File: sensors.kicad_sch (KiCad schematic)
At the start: 7 parts

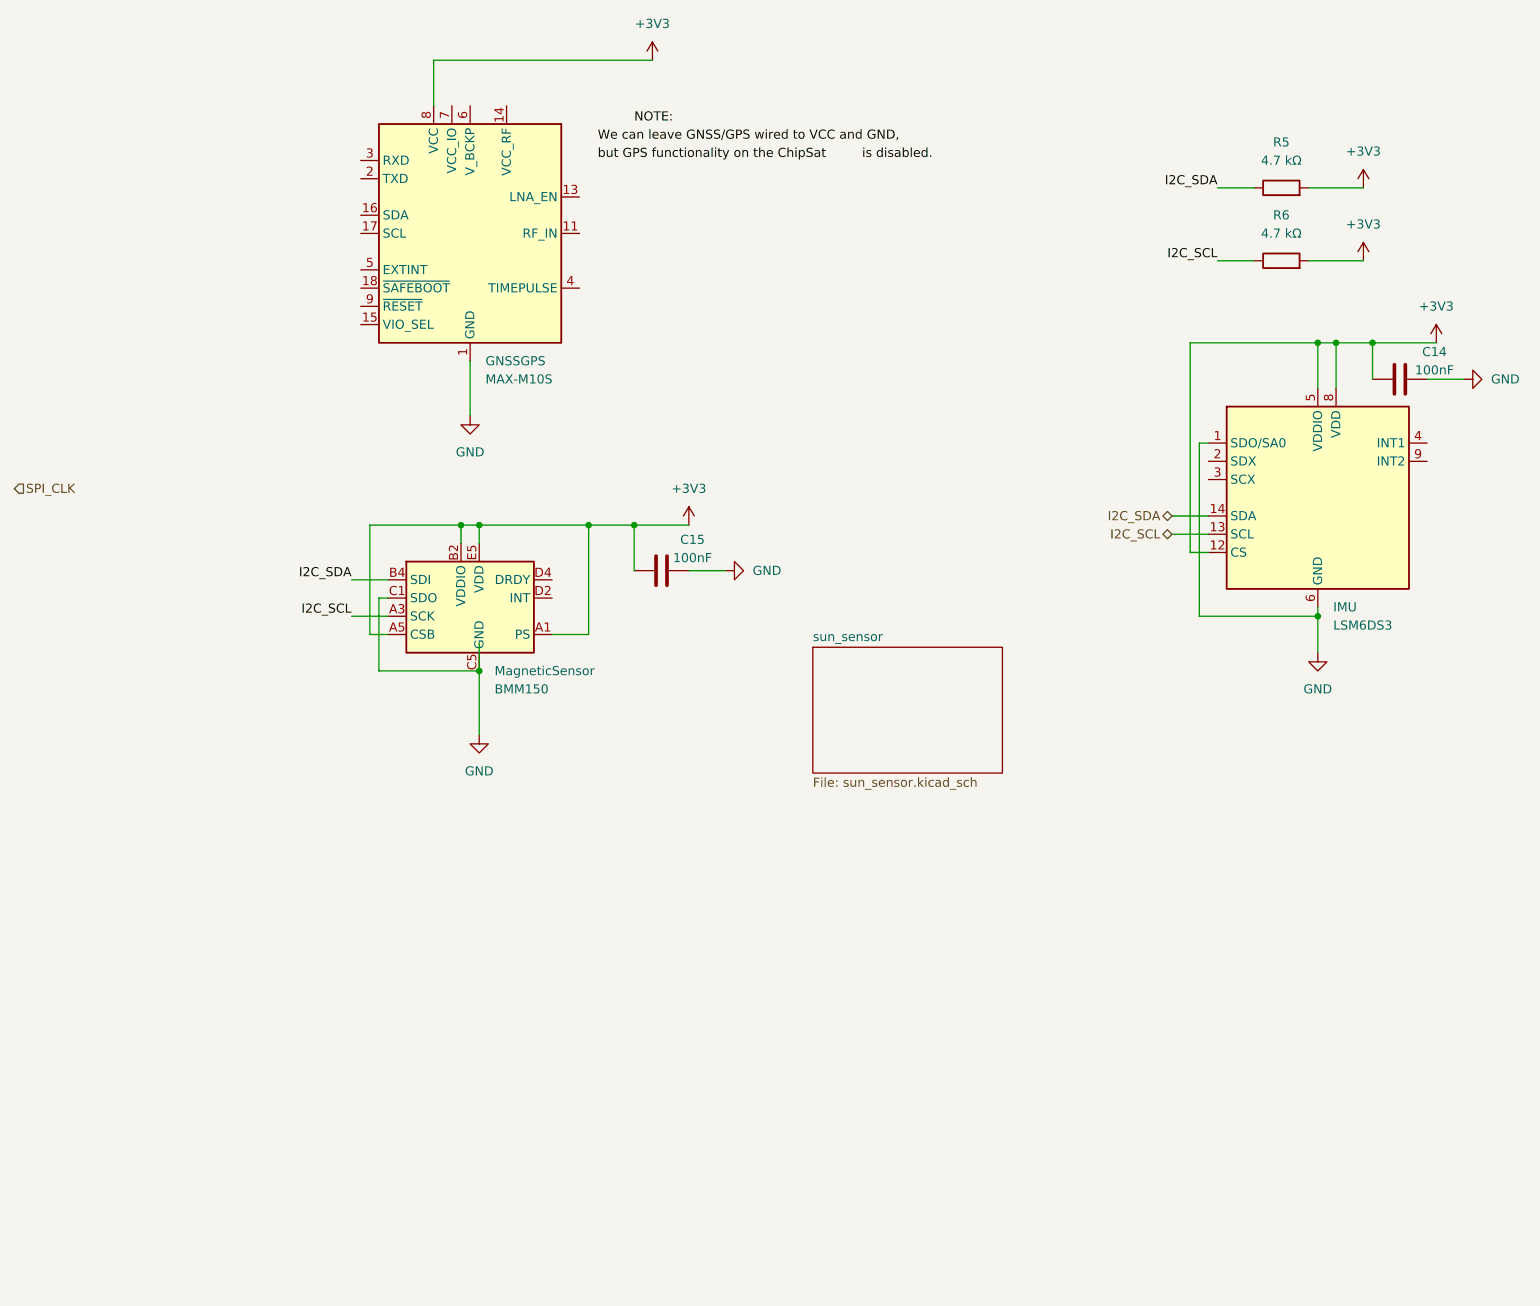
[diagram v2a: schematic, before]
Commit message: Updated GPS, BMI, LSM, and BNO on sensors. Added hierachical labels and new "golden rule" connections
Updated each sensor ensuring they followed the golden rule. I also added hiearchical labels to the topsheet and the inside sheets. Fixed specific sensors to be in SPI vs I2C mode and updated the names.
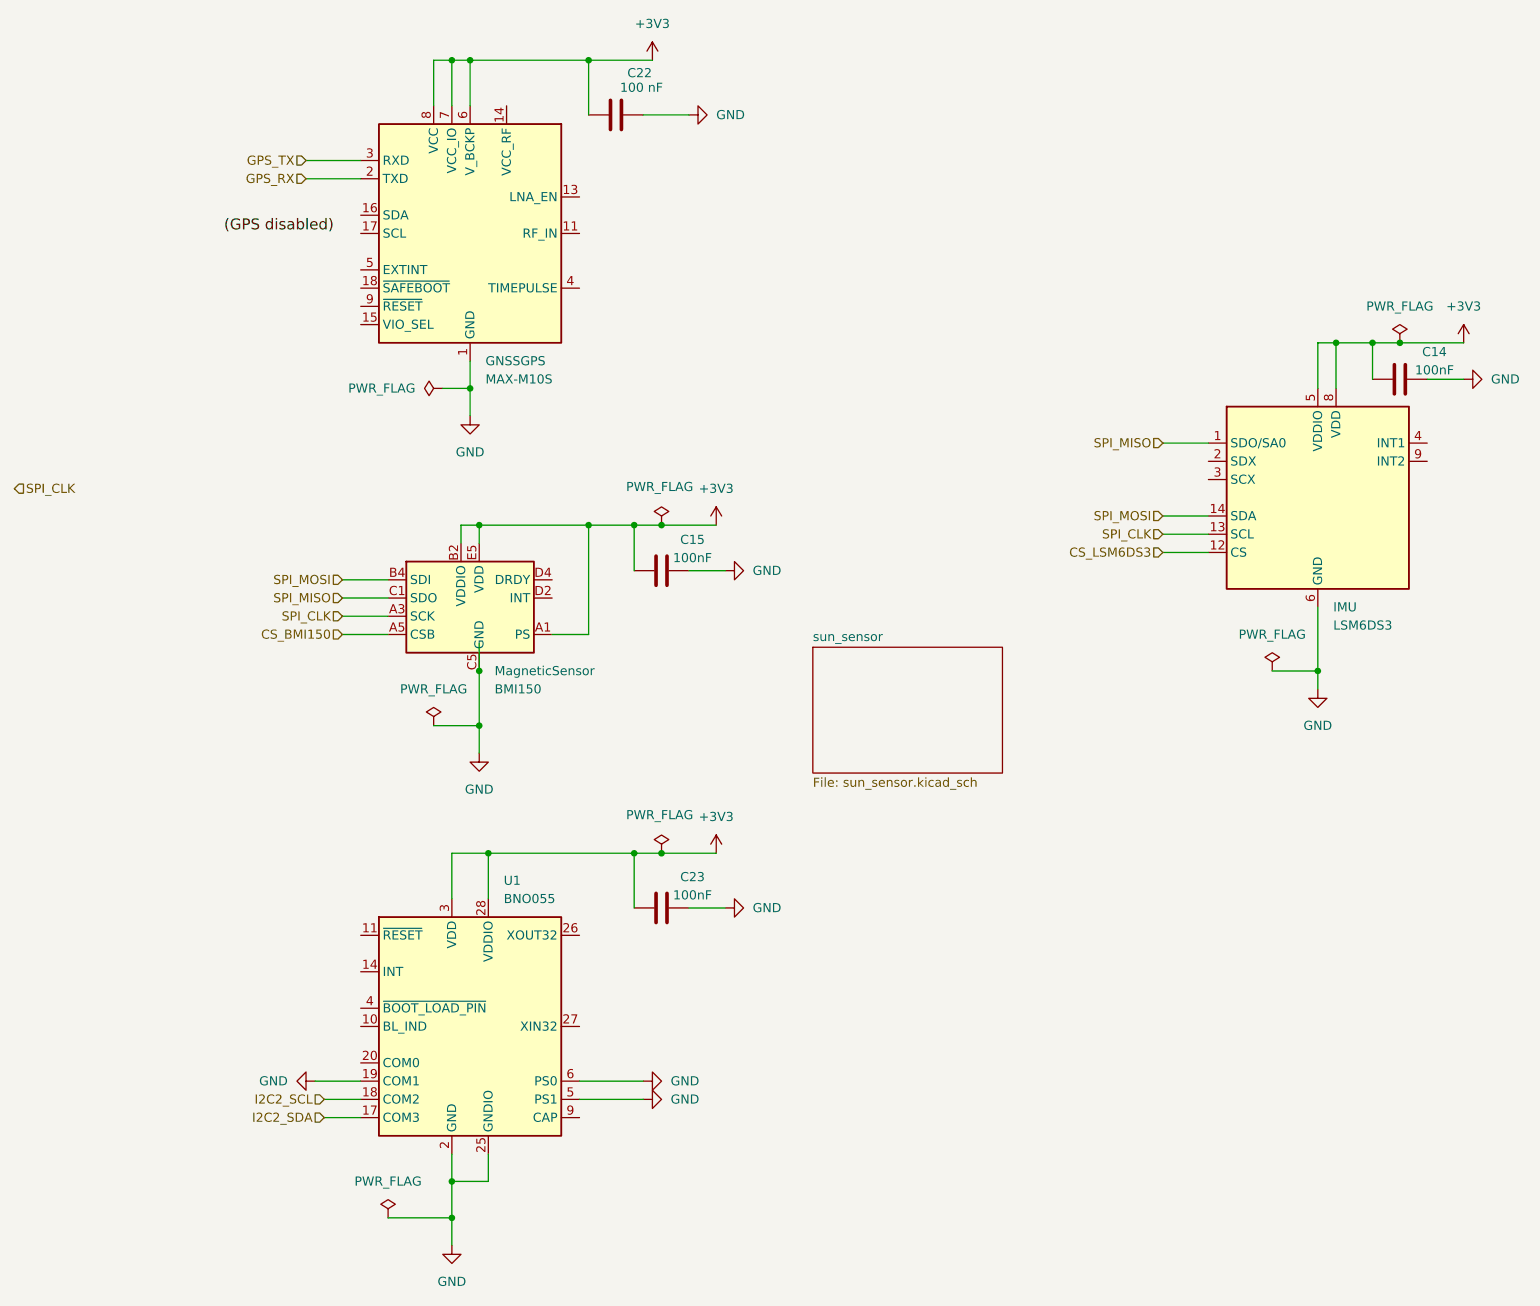
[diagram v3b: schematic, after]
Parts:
- removed R5, R6: 4.7 kΩ, symbol Device:R
- added C22: 100 nF, symbol Device:C
- added C23: 100nF, symbol Device:C
- added U1: BNO055, Package_LGA:LGA-28_5.2x3.8mm_P0.5mm, symbol Sensor_Motion:BNO055
- MagneticSensor: value BMM150 -> BMI150
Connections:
- net I2C_SCL is gone; now on net SPI_CLK: IMU.13 (SCL), MagneticSensor.A3 (SCK)
- net +3V3: now also GNSSGPS.6 (V_BCKP), GNSSGPS.7 (VCC_IO), C22.2, C23.1, U1.28 (VDDIO), U1.3 (VDD); no longer IMU.12 (CS), MagneticSensor.A5 (CSB)
- net GND: now also C22.1, C23.2, U1.19 (COM1), U1.2 (GND), U1.25 (GNDIO), U1.5 (PS1), U1.6 (PS0); no longer IMU.1 (SDO/SA0), MagneticSensor.C1 (SDO)
- net GPS_RX: now reaches GNSSGPS.2 (TXD)
- net GPS_TX: now reaches GNSSGPS.3 (RXD)
- net I2C_SDA renamed SPI_MOSI
- new net CS_BMI150: MagneticSensor.A5 (CSB)
- new net CS_LSM6DS3: IMU.12 (CS)
- new net I2C2_SCL: U1.18 (COM2)
- new net I2C2_SDA: U1.17 (COM3)
- new net SPI_MISO: IMU.1 (SDO/SA0), MagneticSensor.C1 (SDO)

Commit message: Add load switch for sleep rail and IMU interrupt
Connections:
- net IMU_INT1: now reaches IMU.4 (INT1)
- no-connect marks 0 -> 1
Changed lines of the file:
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@@
 		(color 0 0 0 0)
+	)
+	(no_connect
+		(at 236.22 81.28)
 	)
 	(wire
@@
 		)
 	)
+	(hierarchical_label "IMU_INT1"
+		(shape output)
+		(at 236.22 78.74 0)
+		(effects
+			(font
+				(size 1.27 1.27)
+			)
+			(justify left)
+		)
+	)
